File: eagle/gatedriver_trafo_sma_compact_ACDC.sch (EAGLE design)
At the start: 35 parts, among them K1 G5V-2, X4 BU-SMA-V

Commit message: 3PS, 2 1kV in parallel
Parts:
- R10, R11, R4, R7: value 1M -> 10M
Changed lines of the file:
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@@
 <part name="U$1" library="trafo" deviceset="DA-2320" device=""/>
 <part name="C5" library="resistor" deviceset="C-US" device="050-055X075"/>
-<part name="R4" library="rcl" deviceset="R-US_" device="0207/12" value="1M"/>
-<part name="R7" library="rcl" deviceset="R-US_" device="0207/12" value="1M"/>
+<part name="R4" library="rcl" deviceset="R-US_" device="0207/12" value="10M"/>
+<part name="R7" library="rcl" deviceset="R-US_" device="0207/12" value="10M"/>
 <part name="C2" library="resistor" deviceset="C-US" device="050-055X075"/>
 <part name="GND2" library="supply1" deviceset="GND" device=""/>
@@
 <part name="U$7" library="trafo" deviceset="DA-2320" device=""/>
 <part name="C6" library="resistor" deviceset="C-US" device="050-055X075"/>
-<part name="R10" library="rcl" deviceset="R-US_" device="0207/12" value="1M"/>
-<part name="R11" library="rcl" deviceset="R-US_" device="0207/12" value="1M"/>
+<part name="R10" library="rcl" deviceset="R-US_" device="0207/12" value="10M"/>
+<part name="R11" library="rcl" deviceset="R-US_" device="0207/12" value="10M"/>
 <part name="D1" library="diode" deviceset="P6KEXXA" device=""/>
 <part name="D4" library="diode" deviceset="P6KEXXA" device=""/>

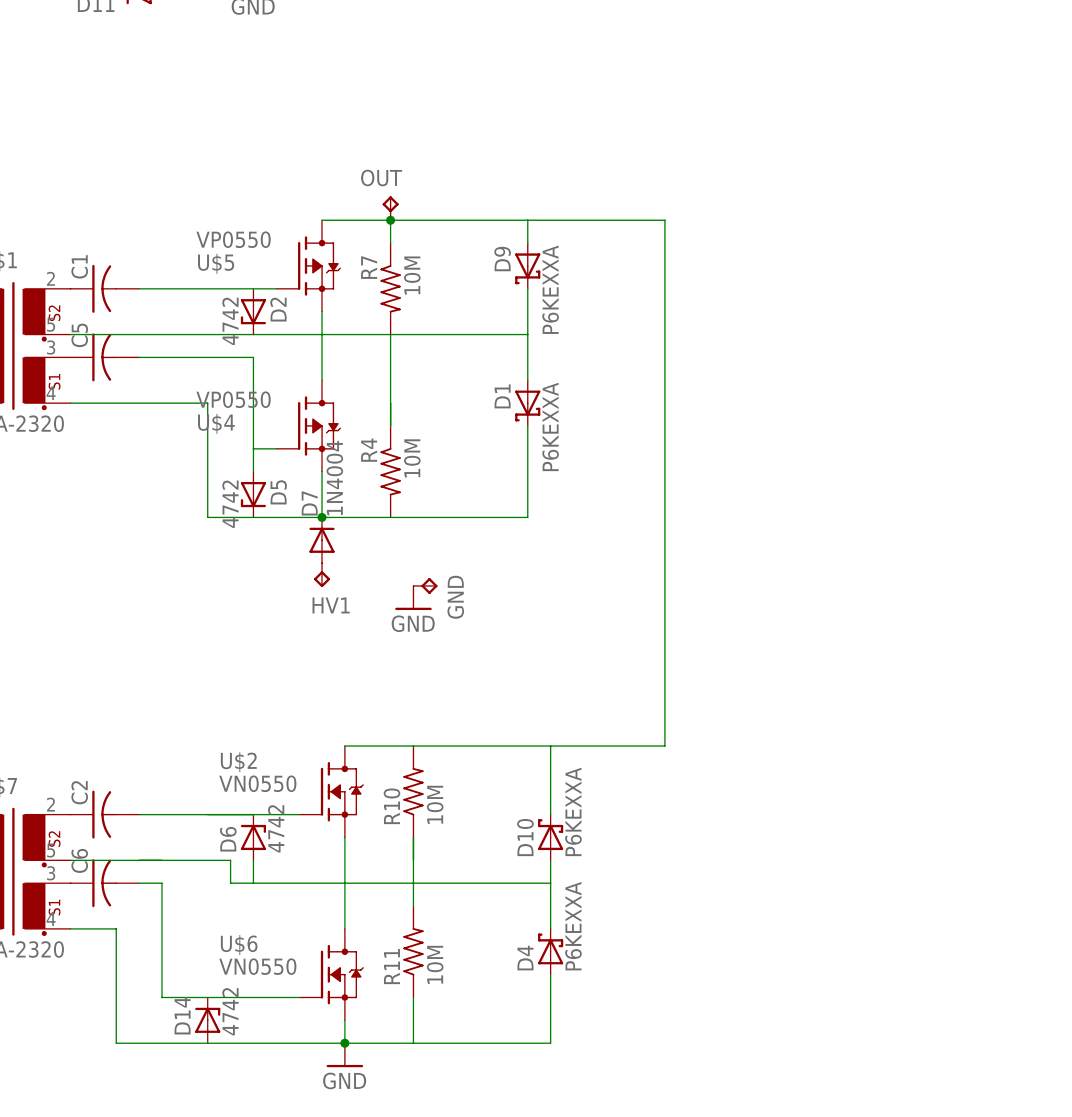
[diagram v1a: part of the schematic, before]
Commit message: capacitor bank
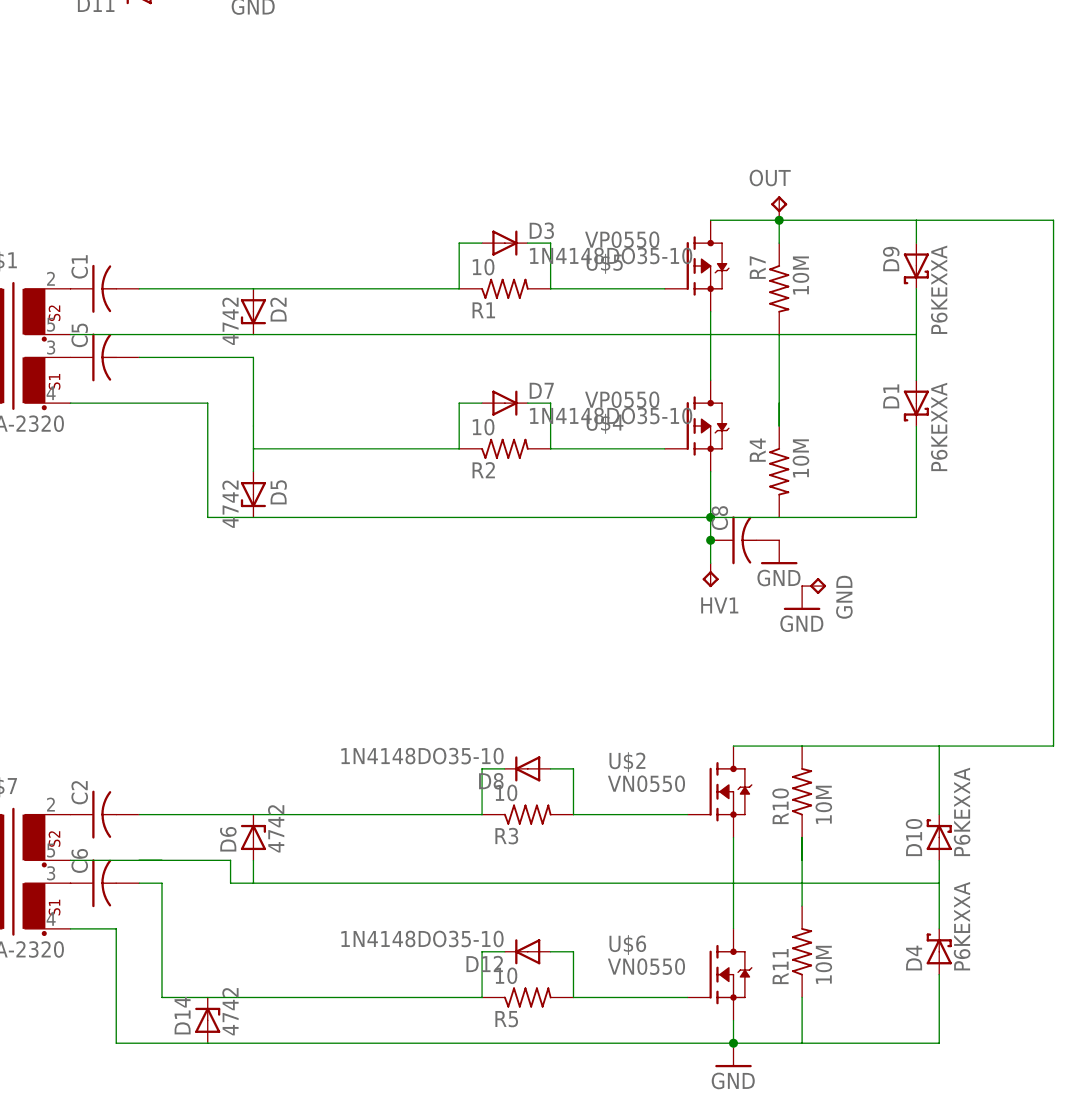
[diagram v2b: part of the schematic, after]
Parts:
- added C8: (no value), rcl:C-US102-054X133
- added D12, D3, D8: 1N4148DO35-10, diode:1N4148DO35-10
- added R1, R2, R3, R5: 10, rcl:R-US_0207/12
- D7: value 1N4004 -> 1N4148DO35-10; device diode:1N4004 -> diode:1N4148DO35-10
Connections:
- removed net N$16: C5.2, D5.A, U$4.G
- removed net N$29: D7.A, HV1.TP
- new net N$10: C1.2, D2.A, D3.A, R1.1
- new net N$12: C5.2, D5.A, D7.A, R2.1
- new net N$19: D8.A, R3.2, U$2.G
- new net N$24: D12.A, R5.2, U$6.G
- new net N$8: D3.C, R1.2, U$5.G
- net GND: now also C8.2
- net N$11: now also D7.C, R2.2, U$4.G; no longer C1.2, D2.A, U$5.G
- net N$17: now also C8.1, HV1.TP; no longer D7.C
- net N$25: now also D8.C, R3.1; no longer U$2.G
- net N$27: now also D12.C, R5.1; no longer U$6.G
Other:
- moved on the sheet: D1, D10, D4, D9, GND, HV1, OUT, R10, R11, R4, R7, U$2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

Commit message: IXYS board solution, gatedriver components
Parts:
- removed D12, D3, D7, D8: 1N4148DO35-10, diode:1N4148DO35-10
- removed GND: TPPAD1-20Y, testpad:TPPAD1-20Y
- added C9: 10p, resistor:C-US102-064X133
- added HV2: TPPAD1-20Y, testpad:TPPAD1-20Y
- added R12, R13, R6, R8, R9: 70, rcl:R-US_0207/10
- added R14: 1M, rcl:R-US_0207/10
- C1, C2, C3, C4, C5, C6: value (none) -> .22u
- C8: value (none) -> 10p; device rcl:C-US102-054X133 -> resistor:C-US102-064X133
- R1, R2, R3, R5: value 10 -> 50k; device rcl:R-US_0207/12 -> rcl:R-US_0207/10
- R10, R11, R4, R7: value 10M -> 1M; device rcl:R-US_0207/12 -> rcl:R-US_0207/10
- U$2, U$6: value VN0550 -> VN0550L; device transistor-fet:VN0550 -> transistor-fet:VN0550L
- U$4, U$5: value VP0550 -> VP0550L; device transistor-fet:VP0550 -> transistor-fet:VP0550L
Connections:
- new net N$16: C5.2, D5.A, R8.1
- new net N$20: C4.2, R14.2
- new net N$251: R3.1, R9.2, U$2.G
- net GND: now also C9.2; no longer D14.A, D4.A, GND.TP, R11.1, U$6.S, U$7.3
- net N$10: now also R6.1; no longer D3.A, R1.1
- net N$11: now also R12.2, R5.1, U$6.G; no longer D7.C, R2.2, U$4.G
- net N$12: now also R8.2, U$4.G; no longer C5.2, D5.A, D7.A
- net N$13: now also R3.2
- net N$17: now also R2.2
- net N$18: now also R1.2
- net N$19: now also C3.2, R13.2; no longer D8.A, R3.2, U$2.G
- net N$24: now also C9.1, D14.A, D4.A, HV2.TP, R11.1, U$6.S, U$7.3; no longer D12.A, U$6.G
- net N$25: now also R9.1; no longer D8.C, R3.1
- net N$27: now also R12.1; no longer D12.C, R5.1
- net N$3: now also R13.1; no longer C3.2
- net N$6: now also R14.1; no longer C4.2
- net N$8: now also R1.1, R6.2; no longer D3.C, R1.2
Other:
- moved on the sheet: C1, C2, C3, C4, C5, C6, C8, D14, D2, D5, D6, K1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

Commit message: 4pcb upload
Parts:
- added D12, D3, D7, D8: 1N4148DO35-10, diode:1N4148DO35-10
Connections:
- net N$10: now also D3.A
- net N$11: now also D12.A
- net N$12: now also D7.C
- net N$16: now also D7.A
- net N$25: now also D8.C
- net N$251: now also D8.A
- net N$27: now also D12.C
- net N$8: now also D3.C

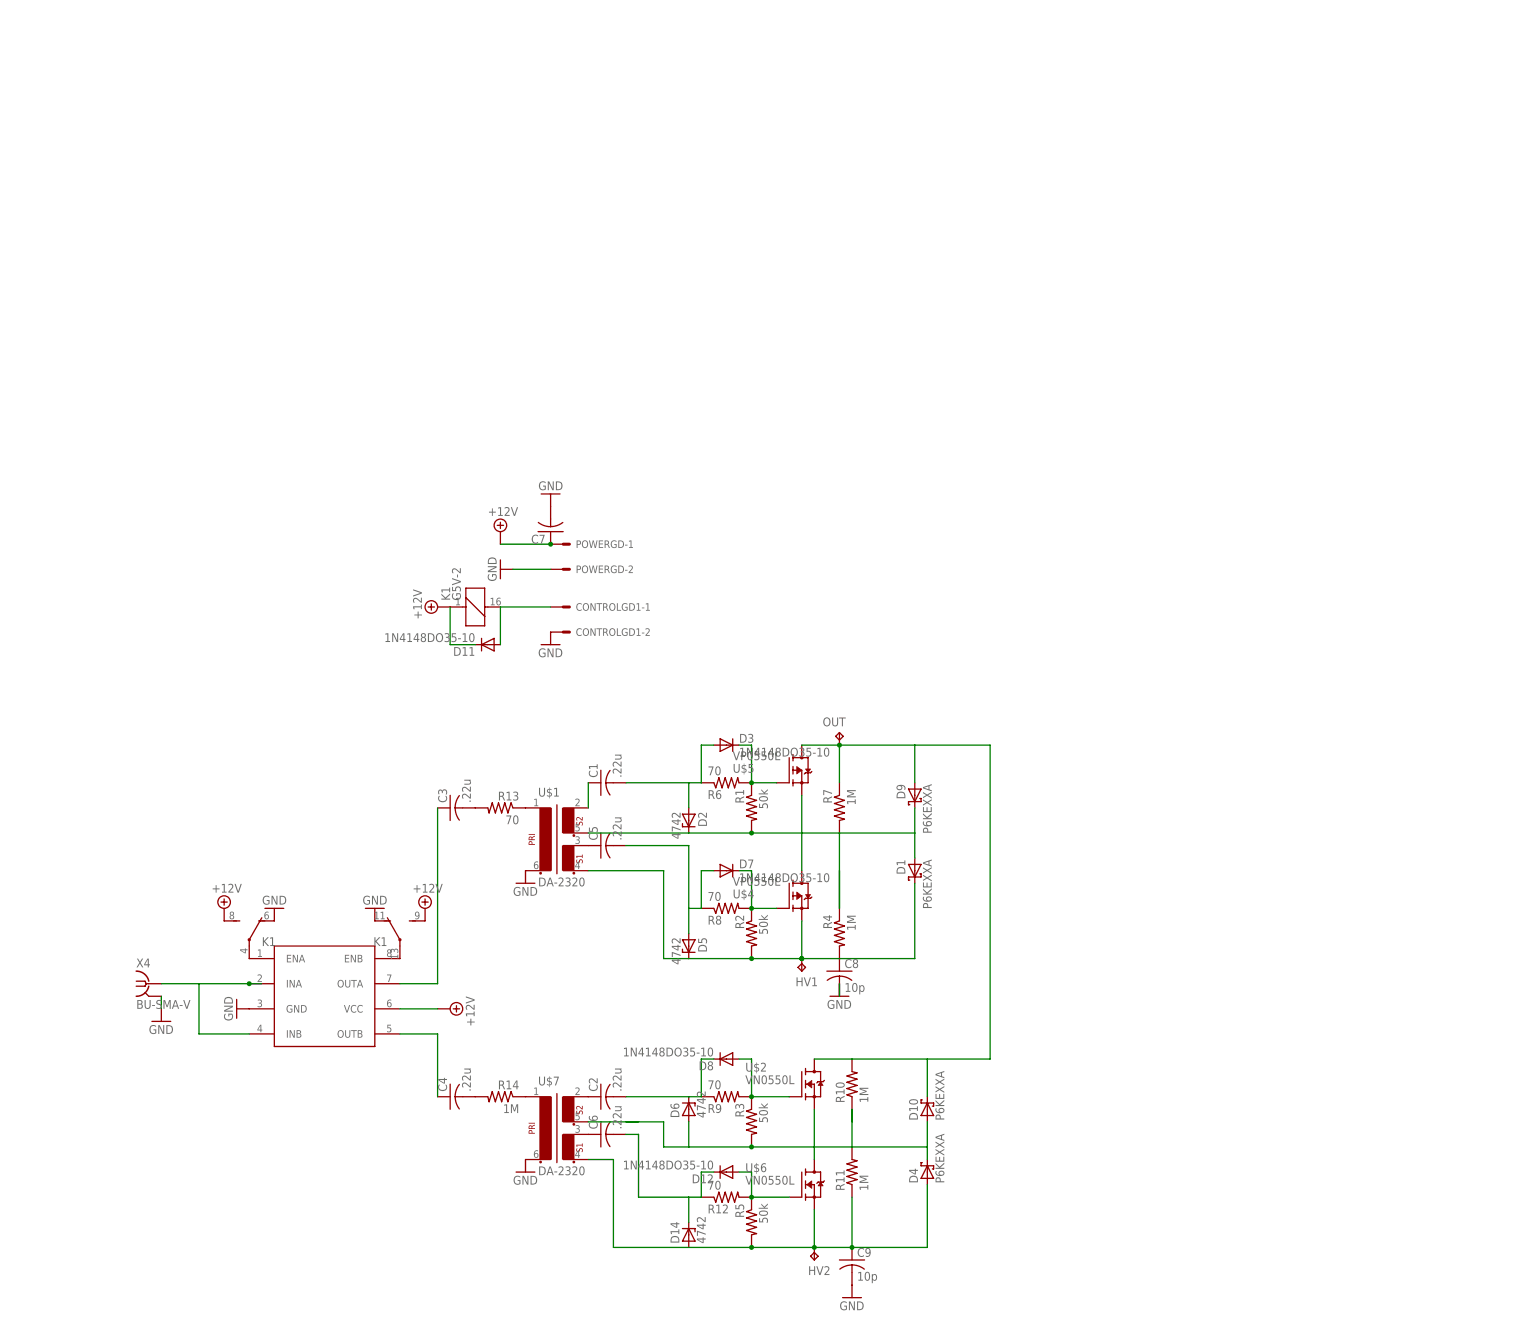
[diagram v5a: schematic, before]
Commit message: optional 317 regulation of emcos
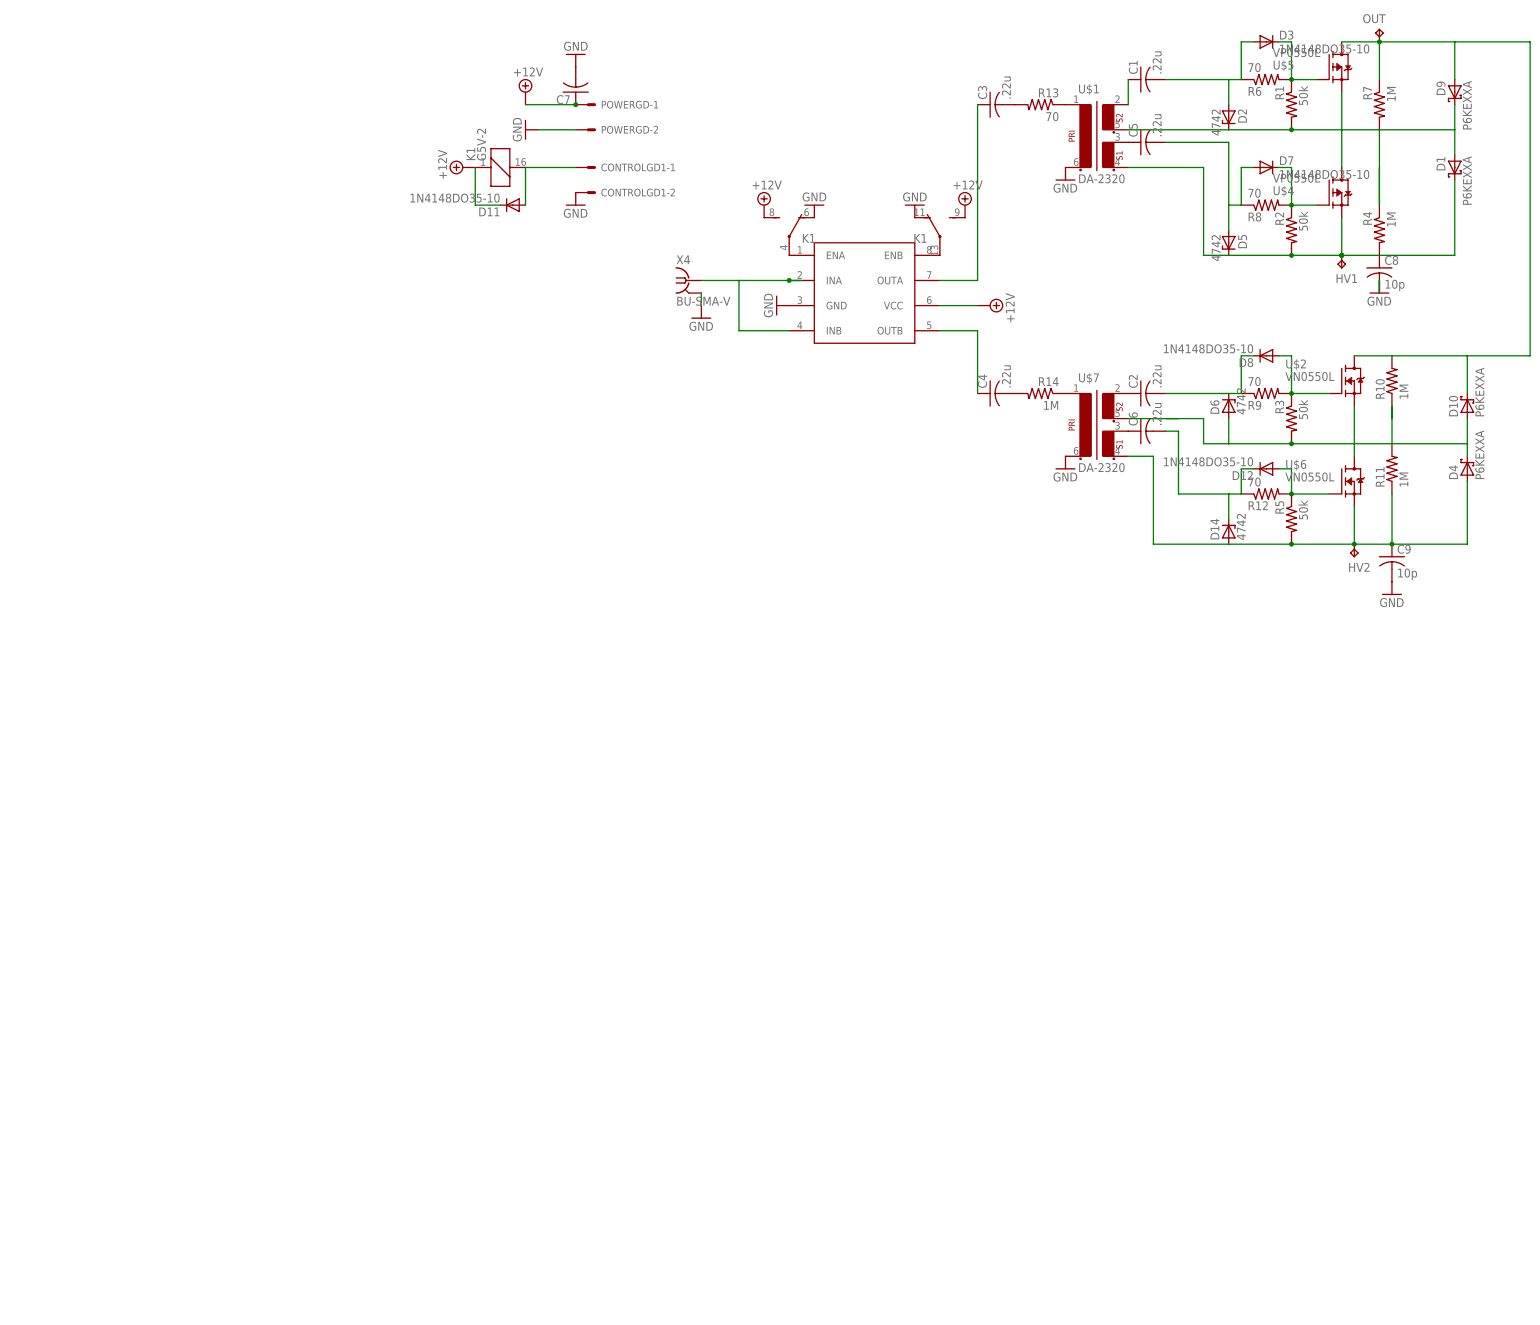
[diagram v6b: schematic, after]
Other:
- moved on the sheet: C1, C2, C3, C4, C5, C6, C7, C8, C9, CONTROLGD1-1, CONTROLGD1-2, D1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

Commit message: timing ctia
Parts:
- added GND1, GND13: TPPAD1-20Y, testpad:TPPAD1-20Y
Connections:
- new net N$26: D1.A, D9.C
- new net N$28: D10.A, D4.C
- net GND: now also GND1.TP, GND13.TP
- net N$13: no longer D10.A, D4.C
- net N$18: no longer D1.A, D9.C
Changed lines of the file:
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@@
 <part name="D12" library="diode" deviceset="1N4148" device="DO35-10"/>
 <part name="FRAME1" library="frames" deviceset="A4L-LOC" device=""/>
+<part name="GND1" library="testpad" deviceset="TP" device="PAD1-20Y"/>
+<part name="GND13" library="testpad" deviceset="TP" device="PAD1-20Y"/>
 </parts>
 <sheets>
@@
 <instance part="R14" gate="G$1" x="142.24" y="91.44" rot="MR0"/>
 <instance part="C8" gate="G$1" x="210.82" y="116.84"/>
-<instance part="GND11" gate="1" x="210.82" y="111.76"/>
+<instance part="GND11" gate="1" x="210.82" y="106.68"/>
 <instance part="HV2" gate="G$1" x="205.74" y="58.42" rot="MR180"/>
 <instance part="C9" gate="G$1" x="213.36" y="58.42"/>
-<instance part="GND5" gate="1" x="213.36" y="50.8"/>
+<instance part="GND5" gate="1" x="213.36" y="45.72"/>
 <instance part="D3" gate="G$1" x="187.96" y="162.56"/>
 <instance part="D7" gate="G$1" x="187.96" y="137.16"/>
@@
 <instance part="D12" gate="G$1" x="187.96" y="76.2" rot="R180"/>
 <instance part="FRAME1" gate="G$1" x="0" y="0"/>
+<instance part="GND1" gate="G$1" x="213.36" y="109.22" rot="MR90"/>
+<instance part="GND13" gate="G$1" x="215.9" y="48.26" rot="MR90"/>
 </instances>
 <busses>
@@
 <pinref part="C8" gate="G$1" pin="2"/>
 <pinref part="GND11" gate="1" pin="GND"/>
-<wire x1="210.82" y1="111.76" x2="210.82" y2="114.3" width="0.1524" layer="91"/>
+<pinref part="GND1" gate="G$1" pin="TP"/>
+<junction x="210.82" y="109.22"/>
+<wire x1="210.82" y1="109.22" x2="210.82" y2="111.76" width="0.1524" layer="91"/>
 </segment>
 <segment>
 <pinref part="C9" gate="G$1" pin="2"/>
 <pinref part="GND5" gate="1" pin="GND"/>
+<pinref part="GND13" gate="G$1" pin="TP"/>
+<pinref part="GND13" gate="G$1" pin="TP"/>
+<junction x="213.36" y="48.26"/>
+<wire x1="213.36" y1="48.26" x2="213.36" y2="53.34" width="0.1524" layer="91"/>
 </segment>
 </net>
@@
 <net name="N$13" class="0">
 <segment>
-<pinref part="D10" gate="1" pin="A"/>
-<pinref part="D4" gate="1" pin="C"/>
-<wire x1="228.6" y1="78.74" x2="228.6" y2="81.28" width="0.1524" layer="91"/>
 <pinref part="D6" gate="G$1" pin="A"/>
 <pinref part="U$2" gate="G$1" pin="S"/>
-<wire x1="228.6" y1="81.28" x2="228.6" y2="86.36" width="0.1524" layer="91"/>
 <wire x1="175.26" y1="86.36" x2="167.64" y2="86.36" width="0.1524" layer="91"/>
 <wire x1="175.26" y1="81.28" x2="175.26" y2="86.36" width="0.1524" layer="91"/>
@@
 <wire x1="205.74" y1="81.28" x2="205.74" y2="88.9" width="0.1524" layer="91"/>
 <wire x1="180.34" y1="86.36" x2="180.34" y2="81.28" width="0.1524" layer="91"/>
-<wire x1="228.6" y1="81.28" x2="213.36" y2="81.28" width="0.1524" layer="91"/>
 <pinref part="R3" gate="G$1" pin="2"/>
 <junction x="193.04" y="81.28"/>
@@
 <wire x1="193.04" y1="144.78" x2="203.2" y2="144.78" width="0.1524" layer="91"/>
 <wire x1="160.02" y1="144.78" x2="180.34" y2="144.78" width="0.1524" layer="91"/>
-<pinref part="D9" gate="1" pin="C"/>
-<pinref part="D1" gate="1" pin="A"/>
-<wire x1="226.06" y1="139.7" x2="226.06" y2="144.78" width="0.1524" layer="91"/>
-<wire x1="226.06" y1="144.78" x2="226.06" y2="149.86" width="0.1524" layer="91"/>
-<wire x1="210.82" y1="144.78" x2="226.06" y2="144.78" width="0.1524" layer="91"/>
 <pinref part="R1" gate="G$1" pin="2"/>
 <junction x="193.04" y="144.78"/>
@@
 </segment>
 </net>
+<net name="N$26" class="0">
+<segment>
+<pinref part="D9" gate="1" pin="C"/>
+<pinref part="D1" gate="1" pin="A"/>
+<wire x1="226.06" y1="139.7" x2="226.06" y2="149.86" width="0.1524" layer="91"/>
+</segment>
+</net>
+<net name="N$28" class="0">
+<segment>
+<pinref part="D10" gate="1" pin="A"/>
+<pinref part="D4" gate="1" pin="C"/>
+<wire x1="228.6" y1="78.74" x2="228.6" y2="86.36" width="0.1524" layer="91"/>
+</segment>
+</net>
